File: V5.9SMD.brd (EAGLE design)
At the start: 85.1 x 50.8 mm, 37 parts, among them IC1 TL084D

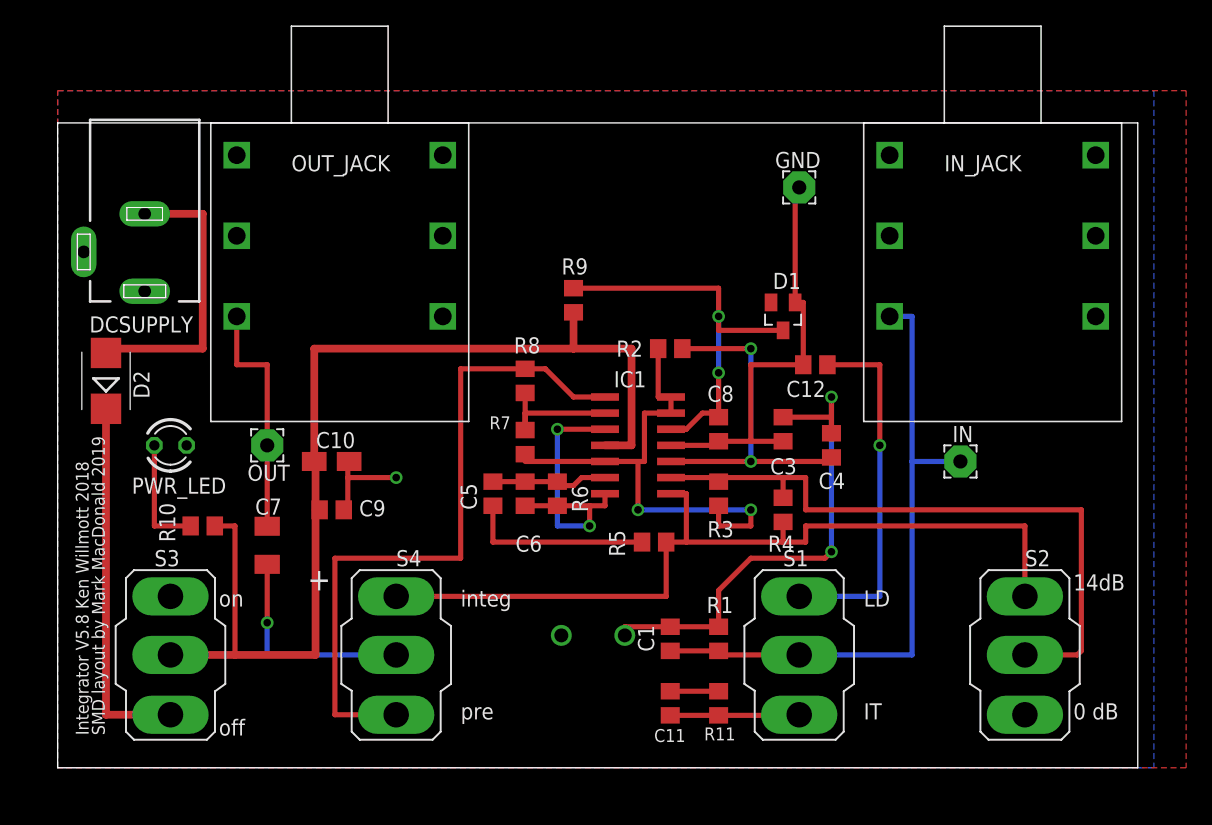
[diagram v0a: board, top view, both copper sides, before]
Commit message: Updated bypass and i/o jacks
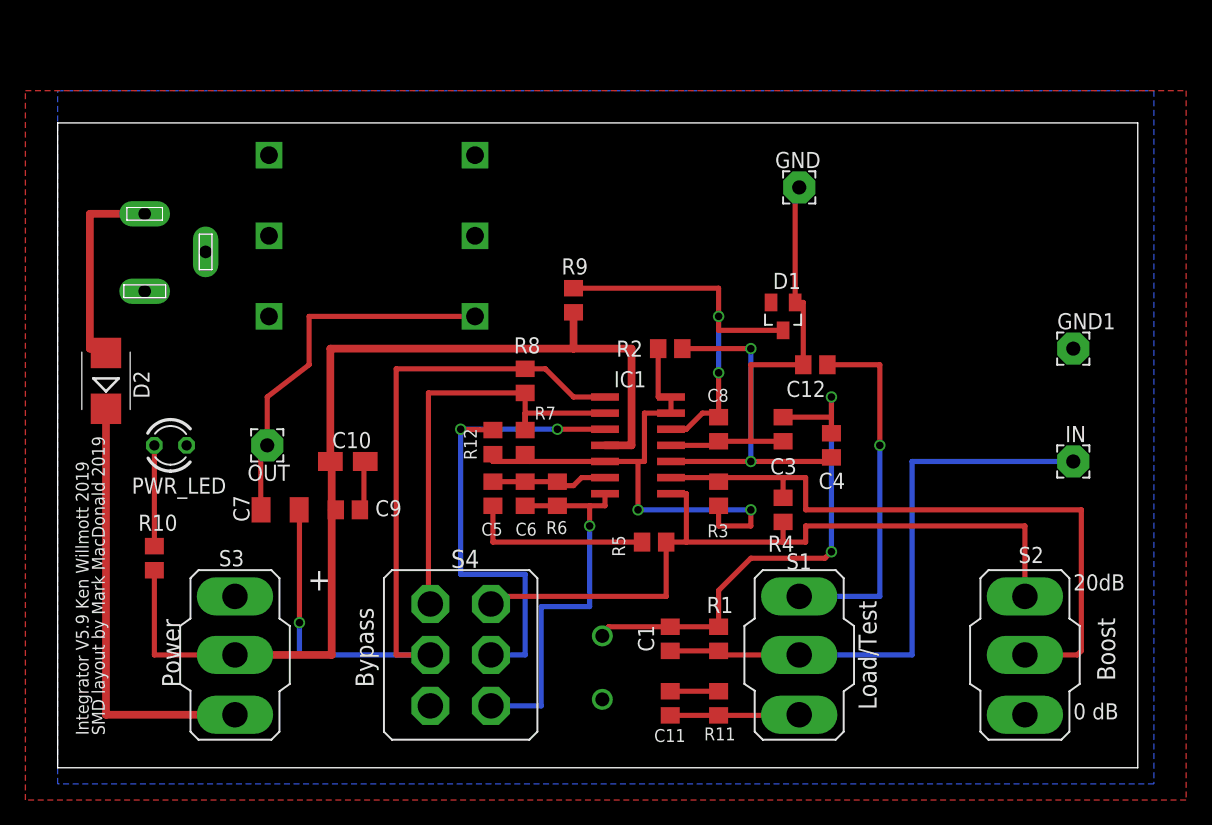
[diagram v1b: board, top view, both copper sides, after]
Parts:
- removed IN_JACK: NMJ6HCD3, Heliostat:AUDIO_JACK_NEUTRIK
- added GND1: (no value), wirepad:2,54/1,1
- added R12: 1.0M, rcl:R0805
- S4: device switch:320-916 -> switch:320-938
- moved IN 8.89 mm to (80.0, 24.1)
- moved S3 5.08 mm to (14.0, 8.89)
- moved S4 5.08 mm to (31.8, 8.89), turned to 180 degrees
- moved R10 4.58 mm to (7.62, 16.5), turned to 270 degrees
- moved C7 2.97 mm to (17.5, 20.3), turned to 180 degrees
- moved C2 2.64 mm to (42.9, 7.89), turned to 90 degrees
- moved OUT_JACK 2.54 mm to (24.8, 41.9), flipped to the bottom
- moved C10 1.27 mm to (22.9, 24.1)
- moved C9 1.27 mm to (22.9, 20.3)
- flipped DCSUPPLY to the bottom
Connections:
- removed net N$13: C1.1, IN.1, IN_JACK.T, R1.1, S1.2
- removed net N$17: C7.1, S4.2
- new net N$11: IC1.3, R12.2, S4.2
- net GND: now also C1.1, GND1.1, IN.1, R1.1, S1.2; no longer IN_JACK.S, IN_JACK.SN
- net N$14: now also R12.1
- net N$4: now also S4.3; no longer S4.1
- net N$6: now also S4.1; no longer IC1.3
- net N$7: now also S4.6
- net N$8: now also C7.1, S4.5; no longer S4.3
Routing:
- net N$13: track 51.4 -> 0.00 mm
- net GND: track 45.9 -> 89.2 mm, vias 1 -> 0
- net N$11: track 0.00 -> 39.5 mm, vias 0 -> 2
- net N$7: track 10.6 -> 35.0 mm
- net N$17: track 17.3 -> 0.00 mm, vias 1 -> 0
- net N$22: track 19.1 -> 30.1 mm
- net N$8: track 54.3 -> 64.4 mm, vias 0 -> 1
- net N$6: track 22.7 -> 30.8 mm, vias 2 -> 1
- net N$4: track 67.2 -> 60.4 mm
- net N$21: track 23.2 -> 16.5 mm
- net N$3: track 29.2 -> 34.3 mm
- net N$15: track 85.3 -> 81.5 mm
- net N$14: track 40.1 -> 43.3 mm
- net N$9: track 39.9 -> 41.4 mm
- net N$1: track 9.21 -> 7.94 mm
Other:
- board text added: "20dB"
- board text added: "Boost"
- board text added: "Bypass"
- board text added: "Integrator V5.9 Ken Willmott 2019"
- board text added: "Load/Test"
- board text added: "Power"
- board text removed: "14dB"
- board text removed: "IT"
- board text removed: "Integrator V5.8 Ken Willmott 2018"
- board text removed: "LD"
- board text removed: "integ"
- board text removed: "off"
- board text removed: "on"
- board text removed: "pre"
